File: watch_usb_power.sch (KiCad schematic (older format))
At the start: 31 parts, among them CON1 USB-MICRO-B, U4 74AHC1G14, U5 LTC4063, U6 FT230XQ, U7 TPS61093

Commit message: Added .gitignore, finished midmount layout
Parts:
- removed C28: 100nF, SMD_Packages:SMD-0603, symbol C
- removed C34: 1uF, SMD_Packages:SMD-0603, symbol C
- CON1: footprint Omat:USB_MICRO_AB_FEMALE -> Omat:USB_MICRO_B_FEMALE_MIDMOUNT
- F1: value PPTC -> MF-FSMF050X-2; footprint SMD_Packages:SMD-0805 -> SMD_Packages:SMD-0603
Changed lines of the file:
@@
 F 0 "CON1" H 1300 2300 50  0000 C CNN
 F 1 "USB-MICRO-B" H 1450 1600 50  0000 C CNN
-F 2 "Omat:USB_MICRO_AB_FEMALE" H 1600 1850 50  0001 C CNN
+F 2 "Omat:USB_MICRO_B_FEMALE_MIDMOUNT" H 1600 1850 50  0001 C CNN
 F 3 "" H 1600 1850 50  0000 C CNN
 	1    1600 1950
@@
 P 2650 1400
 F 0 "F1" H 2750 1450 40  0000 C CNN
-F 1 "PPTC" H 2550 1350 40  0000 C CNN
-F 2 "SMD_Packages:SMD-0805" H 2650 1400 60  0001 C CNN
+F 1 "MF-FSMF050X-2" H 2550 1350 40  0000 C CNN
+F 2 "SMD_Packages:SMD-0603" H 2650 1400 60  0001 C CNN
 F 3 "" H 2650 1400 60  0000 C CNN
 	1    2650 1400
@@
 Text Label 3500 2300 0    60   ~ 0
 VBUS
-$Comp
-L C C28
-U 1 1 5459F911
-P 4200 2650
-F 0 "C28" H 4200 2750 40  0000 L CNN
-F 1 "100nF" H 4206 2565 40  0000 L CNN
-F 2 "SMD_Packages:SMD-0603" H 4238 2500 30  0001 C CNN
-F 3 "" H 4200 2650 60  0000 C CNN
-	1    4200 2650
-	1    0    0    -1
-$EndComp
 $Comp
 L CP2 C27
@@
 	4800 2100 4500 2100
 Connection ~ 4500 2300
-Wire Wire Line
-	4200 2200 4800 2200
 Connection ~ 4500 2200
 Wire Wire Line
@@
 Connection ~ 4750 2550
 Wire Wire Line
-	4750 2950 4200 2950
-Wire Wire Line
 	4500 2850 4500 3050
 Connection ~ 4500 2950
@@
 	3500 2950 3500 3000
 Connection ~ 3500 2950
-Wire Wire Line
-	4200 2200 4200 2450
-Wire Wire Line
-	4200 2950 4200 2850
 Wire Wire Line
 	4500 2300 4800 2300
@@
 	7500 4950 7500 5200
 Wire Wire Line
-	7500 5200 10300 5200
-Wire Wire Line
 	7800 4900 7800 5200
 Connection ~ 7800 5200
@@
 Wire Wire Line
 	10200 3750 10200 3850
-Wire Wire Line
-	9350 3950 10450 3950
 Wire Wire Line
 	9350 4050 9650 4050
@@
 Connection ~ 9450 5200
 Connection ~ 9950 3950
-Connection ~ 9950 5200
 Wire Wire Line
 	8350 3900 8100 3900
@@
 	9350 4250 9450 4250
 Connection ~ 9450 4250
-Connection ~ 10300 3950
-Wire Wire Line
-	10300 3950 10300 4350
-Wire Wire Line
-	10300 5200 10300 4750
-$Comp
-L C C34
-U 1 1 545C5D16
-P 10300 4550
-F 0 "C34" H 10300 4650 40  0000 L CNN
-F 1 "1uF" H 10306 4465 40  0000 L CNN
-F 2 "SMD_Packages:SMD-0603" H 10338 4400 30  0001 C CNN
-F 3 "" H 10300 4550 60  0000 C CNN
-	1    10300 4550
-	1    0    0    -1
-$EndComp
+Wire Wire Line
+	4750 2950 4500 2950
+Wire Wire Line
+	4500 2200 4800 2200
+Wire Wire Line
+	9350 3950 10450 3950
+Wire Wire Line
+	7500 5200 9950 5200
 $EndSCHEMATC

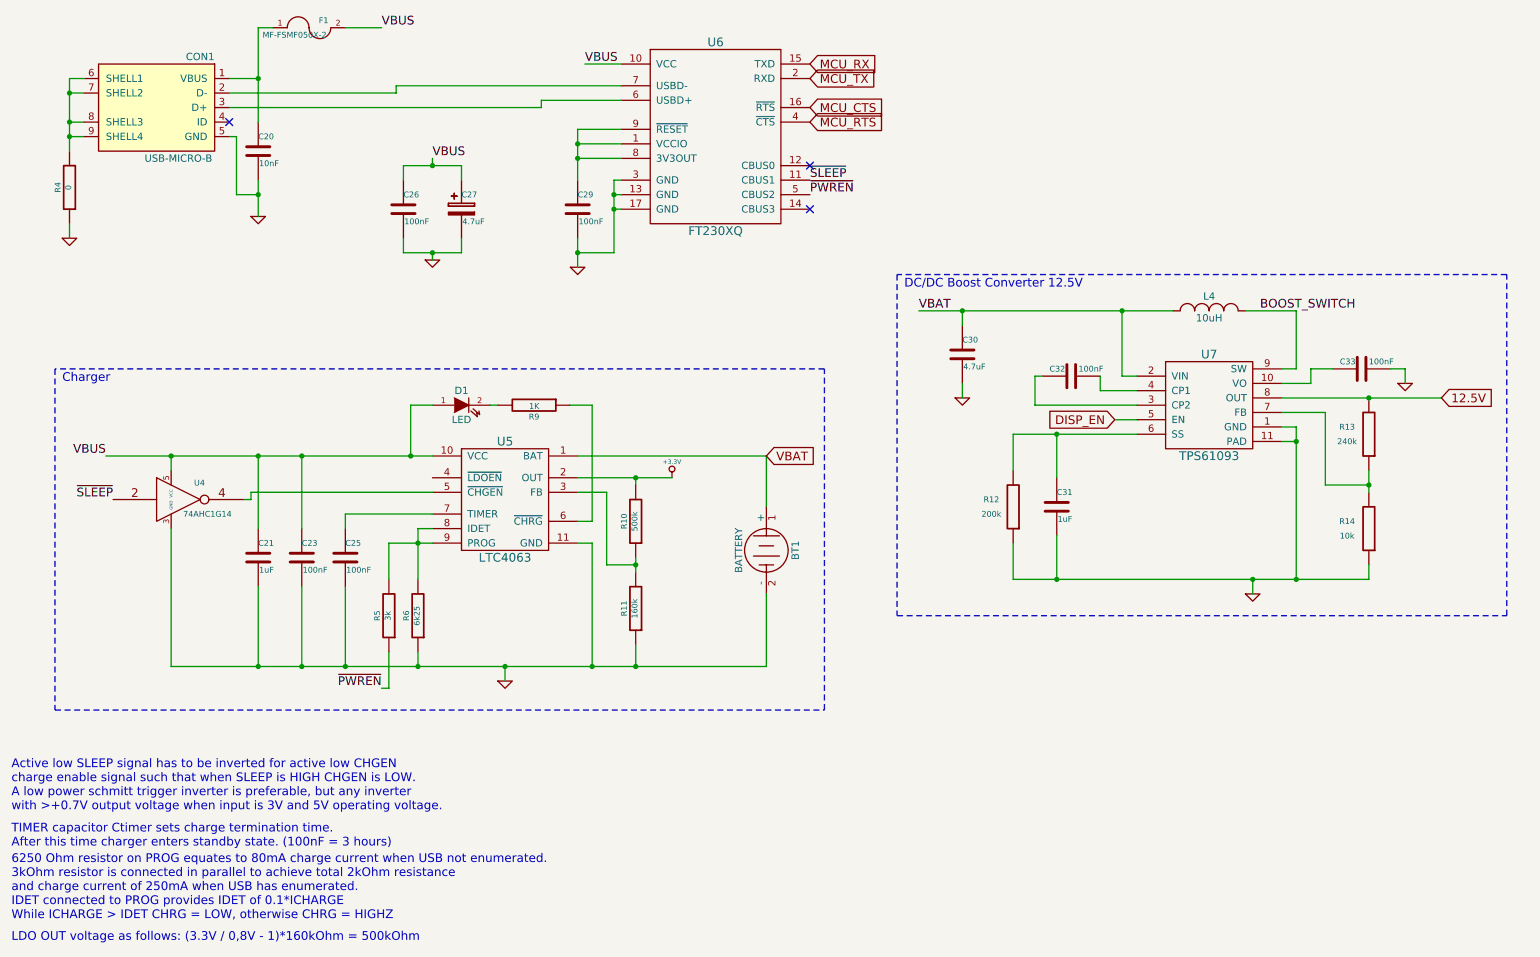
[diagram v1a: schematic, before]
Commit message: Added testpoints, adjusted silkscreen texts
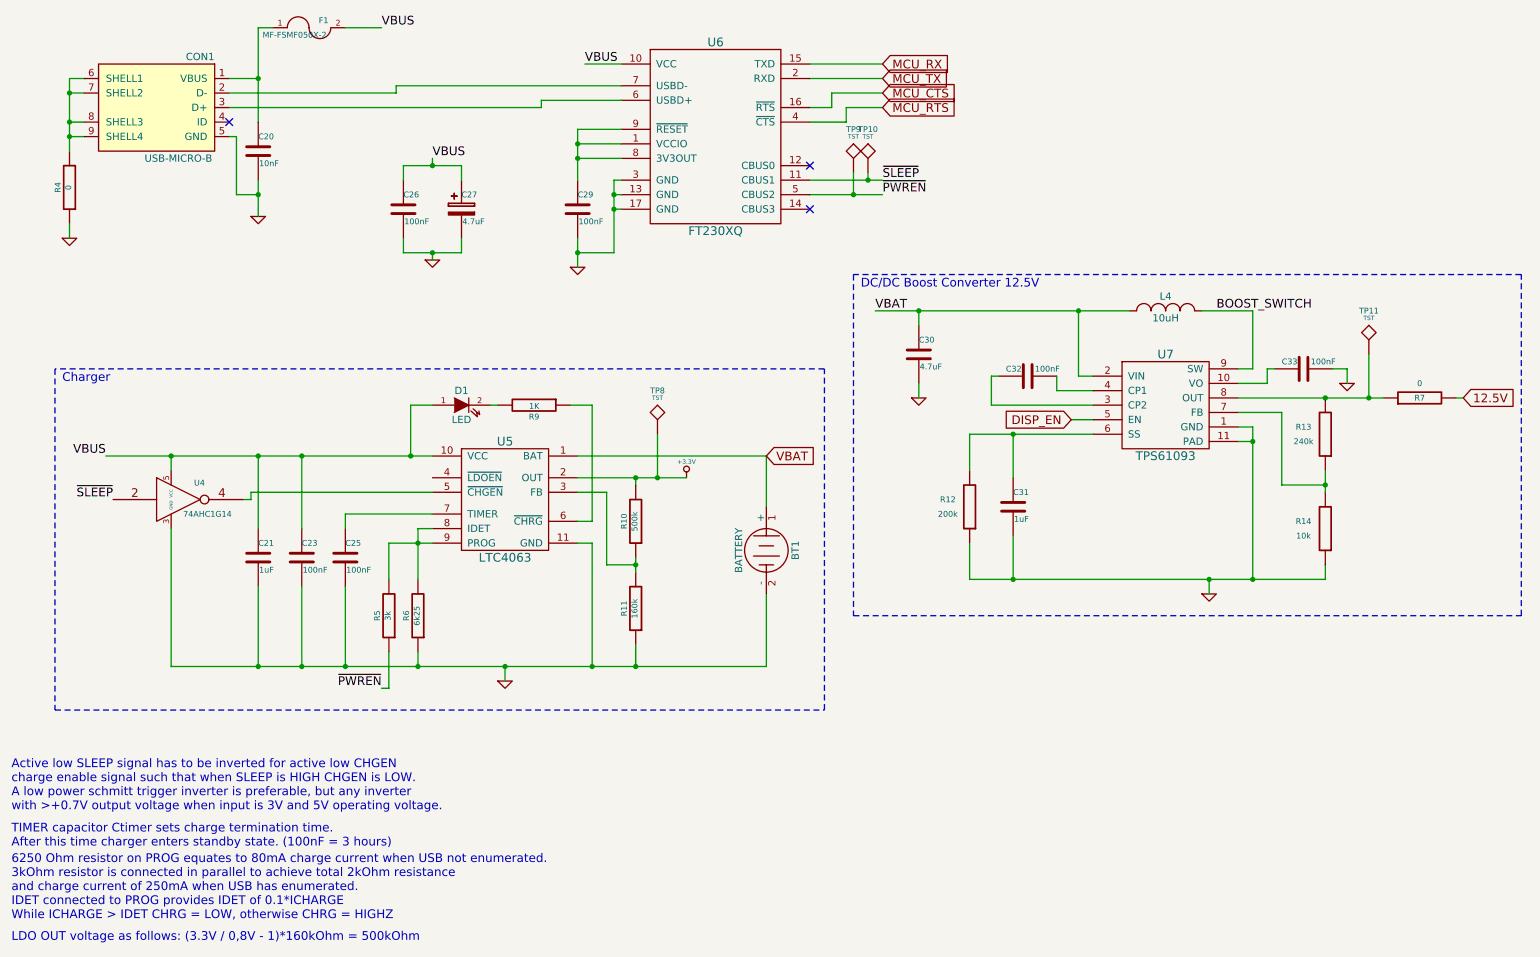
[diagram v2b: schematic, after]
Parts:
- added R7: 0, SMD_Packages:SMD-0603, symbol R
- added TP10, TP11, TP8, TP9: TST, Measurement_Points:Measurement_Point_Round-SMD-Pad_Small, symbol TST
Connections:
- net +3.3V: now also TP8.1
- net 12.5V: now also R7.2; no longer R13.2, U7.8 (OUT)
- net ~PWREN: now also TP9.1
- net ~SLEEP: now also TP10.1
- new net: R13.2, R7.1, TP11.1, U7.8 (OUT)
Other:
- moved on the sheet: C30, C31, C32, C33, L4, R12, R13, R14, U7

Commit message: Added missing 2.2uF cap to LTC4063 LDO output, normalized capacitor values to micro and pico, removed units from component values
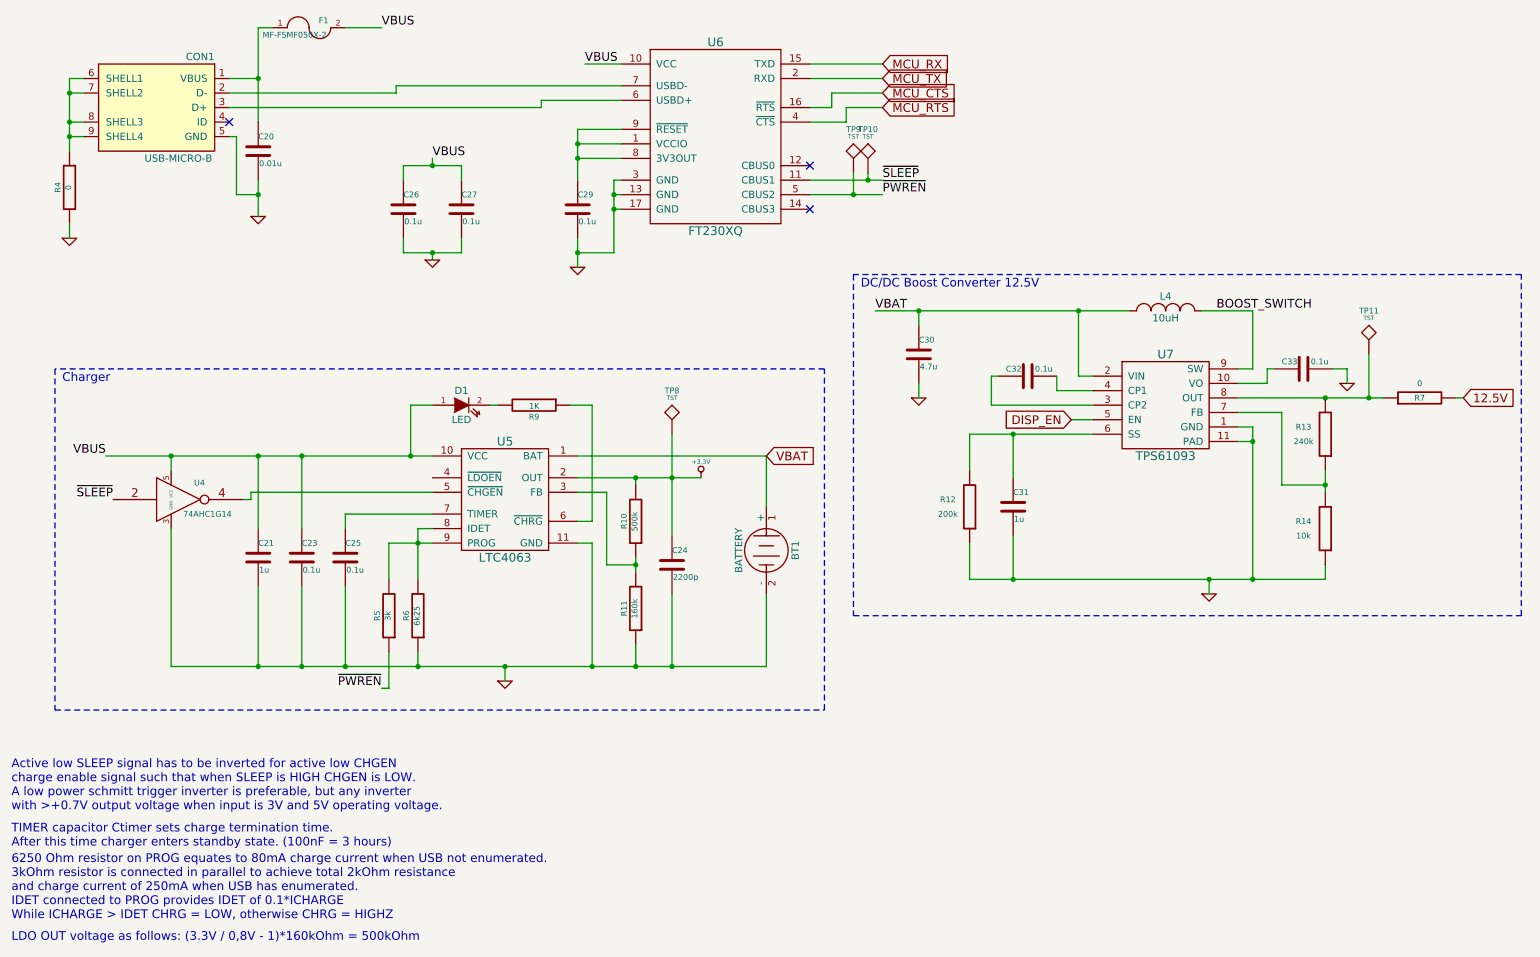
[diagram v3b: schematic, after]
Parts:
- removed C27: 4.7uF, SMD_Packages:SMD-0603, symbol CP2
- added C24: 2200p, SMD_Packages:SMD-0603, symbol C
- added C27: 0.1u, SMD_Packages:SMD-0603, symbol C
- C20: value 10nF -> 0.01u
- C21, C31: value 1uF -> 1u
- C23, C25, C26, C29, C32, C33: value 100nF -> 0.1u
- C30: value 4.7uF -> 4.7u
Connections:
- net +3.3V: now also C24.1
- net GND: now also C24.2, C27.2
- net VBUS: now also C27.1
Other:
- moved on the sheet: TP8
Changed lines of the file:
@@
 P 2300 2250
 F 0 "C20" H 2300 2350 40  0000 L CNN
-F 1 "10nF" H 2306 2165 40  0000 L CNN
+F 1 "0.01u" H 2306 2165 40  0000 L CNN
 F 2 "SMD_Packages:SMD-0603" H 2338 2100 30  0001 C CNN
 F 3 "" H 2300 2250 60  0000 C CNN
@@
 P 4500 2650
 F 0 "C29" H 4500 2750 40  0000 L CNN
-F 1 "100nF" H 4506 2565 40  0000 L CNN
+F 1 "0.1u" H 4506 2565 40  0000 L CNN
 F 2 "SMD_Packages:SMD-0603" H 4538 2500 30  0001 C CNN
 F 3 "" H 4500 2650 60  0000 C CNN
@@
 P 3300 2650
 F 0 "C26" H 3300 2750 40  0000 L CNN
-F 1 "100nF" H 3306 2565 40  0000 L CNN
+F 1 "0.1u" H 3306 2565 40  0000 L CNN
 F 2 "SMD_Packages:SMD-0603" H 3338 2500 30  0001 C CNN
 F 3 "" H 3300 2650 60  0000 C CNN
@@
 VBUS
 $Comp
-L CP2 C27
-U 1 1 5459FD49
-P 3700 2650
-F 0 "C27" H 3700 2750 40  0000 L CNN
-F 1 "4.7uF" H 3706 2565 40  0000 L CNN
-F 2 "SMD_Packages:SMD-0603" H 3738 2500 30  0001 C CNN
-F 3 "" H 3700 2650 60  0000 C CNN
-	1    3700 2650
-	1    0    0    -1
-$EndComp
-$Comp
 L C C23
 U 1 1 545A029E
 P 2600 5050
 F 0 "C23" H 2600 5150 40  0000 L CNN
-F 1 "100nF" H 2606 4965 40  0000 L CNN
+F 1 "0.1u" H 2606 4965 40  0000 L CNN
 F 2 "SMD_Packages:SMD-0603" H 2638 4900 30  0001 C CNN
 F 3 "" H 2600 5050 60  0000 C CNN
@@
 P 2900 5050
 F 0 "C25" H 2900 5150 40  0000 L CNN
-F 1 "100nF" H 2906 4965 40  0000 L CNN
+F 1 "0.1u" H 2906 4965 40  0000 L CNN
 F 2 "SMD_Packages:SMD-0603" H 2938 4900 30  0001 C CNN
 F 3 "" H 2900 5050 60  0000 C CNN
@@
 P 2300 5050
 F 0 "C21" H 2300 5150 40  0000 L CNN
-F 1 "1uF" H 2306 4965 40  0000 L CNN
+F 1 "1u" H 2306 4965 40  0000 L CNN
 F 2 "SMD_Packages:SMD-0603" H 2338 4900 30  0001 C CNN
 F 3 "" H 2300 5050 60  0000 C CNN
@@
 P 6850 3650
 F 0 "C30" H 6850 3750 40  0000 L CNN
-F 1 "4.7uF" H 6856 3565 40  0000 L CNN
+F 1 "4.7u" H 6856 3565 40  0000 L CNN
 F 2 "SMD_Packages:SMD-0603" H 6888 3500 30  0001 C CNN
 F 3 "" H 6850 3650 60  0000 C CNN
@@
 P 7600 3800
 F 0 "C32" V 7550 3650 40  0000 L CNN
-F 1 "100nF" V 7550 3850 40  0000 L CNN
+F 1 "0.1u" V 7550 3850 40  0000 L CNN
 F 2 "SMD_Packages:SMD-0603" H 7638 3650 30  0001 C CNN
 F 3 "" H 7600 3800 60  0000 C CNN
@@
 P 7500 4700
 F 0 "C31" H 7500 4800 40  0000 L CNN
-F 1 "1uF" H 7506 4615 40  0000 L CNN
+F 1 "1u" H 7506 4615 40  0000 L CNN
 F 2 "SMD_Packages:SMD-0603" H 7538 4550 30  0001 C CNN
 F 3 "" H 7500 4700 60  0000 C CNN
@@
 P 9500 3750
 F 0 "C33" V 9450 3600 40  0000 L CNN
-F 1 "100nF" V 9450 3800 40  0000 L CNN
+F 1 "0.1u" V 9450 3800 40  0000 L CNN
 F 2 "SMD_Packages:SMD-0603" H 9538 3600 30  0001 C CNN
 F 3 "" H 9500 3750 60  0000 C CNN
@@
 L +3.3V #PWR024
 U 1 1 546AD98B
-P 5250 4500
-F 0 "#PWR024" H 5250 4460 30  0001 C CNN
-F 1 "+3.3V" H 5250 4610 30  0000 C CNN
-F 2 "" H 5250 4500 60  0000 C CNN
-F 3 "" H 5250 4500 60  0000 C CNN
-	1    5250 4500
+P 5350 4500
+F 0 "#PWR024" H 5350 4460 30  0001 C CNN
+F 1 "+3.3V" H 5350 4610 30  0000 C CNN
+F 2 "" H 5350 4500 60  0000 C CNN
+F 3 "" H 5350 4500 60  0000 C CNN
+	1    5350 4500
 	1    0    0    -1
 $EndComp
@@
 	4900 4500 4900 4550
 Wire Wire Line
-	4500 4500 5250 4500
+	4500 4500 5350 4500
 Wire Wire Line
 	4500 4600 4700 4600
@@
 L TST TP8
 U 1 1 54824541
-P 5050 4200
-F 0 "TP8" H 5050 4500 40  0000 C CNN
-F 1 "TST" H 5050 4450 30  0000 C CNN
-F 2 "Measurement_Points:Measurement_Point_Round-SMD-Pad_Small" H 5050 4200 60  0001 C CNN
-F 3 "" H 5050 4200 60  0000 C CNN
-	1    5050 4200
-	1    0    0    -1
-$EndComp
-Wire Wire Line
-	5050 4200 5050 4500
-Connection ~ 5050 4500
+P 5150 4200
+F 0 "TP8" H 5150 4500 40  0000 C CNN
+F 1 "TST" H 5150 4450 30  0000 C CNN
+F 2 "Measurement_Points:Measurement_Point_Round-SMD-Pad_Small" H 5150 4200 60  0001 C CNN
+F 3 "" H 5150 4200 60  0000 C CNN
+	1    5150 4200
+	1    0    0    -1
+$EndComp
+Wire Wire Line
+	5150 4200 5150 4900
+Connection ~ 5150 4500
 $Comp
 L TST TP11
@@
 	0    -1   -1   0
 $EndComp
+$Comp
+L C C24
+U 1 1 54839CDB
+P 5150 5100
+F 0 "C24" H 5150 5200 40  0000 L CNN
+F 1 "2200p" H 5156 5015 40  0000 L CNN
+F 2 "SMD_Packages:SMD-0603" H 5188 4950 30  0001 C CNN
+F 3 "" H 5150 5100 60  0000 C CNN
+	1    5150 5100
+	1    0    0    -1
+$EndComp
+Wire Wire Line
+	5150 5300 5150 5800
+Connection ~ 5150 5800
+$Comp
+L C C27
+U 1 1 5483AE74
+P 3700 2650
+F 0 "C27" H 3700 2750 40  0000 L CNN
+F 1 "0.1u" H 3706 2565 40  0000 L CNN
+F 2 "SMD_Packages:SMD-0603" H 3738 2500 30  0001 C CNN
+F 3 "" H 3700 2650 60  0000 C CNN
+	1    3700 2650
+	1    0    0    -1
+$EndComp
 $EndSCHEMATC

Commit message: Fixed footprints for MCU and USB-UART, added testpoints
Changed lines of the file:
@@
 EESchema Schematic File Version 2
+LIBS:watch-rescue
 LIBS:power
 LIBS:device
@@
 $EndComp
 $Comp
-L GND #PWR016
+L GND-RESCUE-watch #PWR016
 U 1 1 5459B57E
 P 2300 2700
+AR Path="/5459B57E" Ref="#PWR016"  Part="1"
+AR Path="/5459B076/5459B57E" Ref="#PWR016"  Part="1"
 F 0 "#PWR016" H 2300 2700 30  0001 C CNN
 F 1 "GND" H 2300 2630 30  0001 C CNN
@@
 $EndComp
 $Comp
-L GND #PWR017
+L GND-RESCUE-watch #PWR017
 U 1 1 5459E8BE
 P 4500 3050
+AR Path="/5459E8BE" Ref="#PWR017"  Part="1"
+AR Path="/5459B076/5459E8BE" Ref="#PWR017"  Part="1"
 F 0 "#PWR017" H 4500 3050 30  0001 C CNN
 F 1 "GND" H 4500 2980 30  0001 C CNN
@@
 $EndComp
 $Comp
-L GND #PWR018
+L GND-RESCUE-watch #PWR018
 U 1 1 5459F2E2
 P 3500 3000
+AR Path="/5459F2E2" Ref="#PWR018"  Part="1"
+AR Path="/5459B076/5459F2E2" Ref="#PWR018"  Part="1"
 F 0 "#PWR018" H 3500 3000 30  0001 C CNN
 F 1 "GND" H 3500 2930 30  0001 C CNN
@@
 $EndComp
 $Comp
-L GND #PWR019
+L GND-RESCUE-watch #PWR019
 U 1 1 545A06F4
 P 1000 2850
+AR Path="/545A06F4" Ref="#PWR019"  Part="1"
+AR Path="/5459B076/545A06F4" Ref="#PWR019"  Part="1"
 F 0 "#PWR019" H 1000 2850 30  0001 C CNN
 F 1 "GND" H 1000 2780 30  0001 C CNN
@@
 $EndComp
 $Comp
-L GND #PWR020
+L GND-RESCUE-watch #PWR020
 U 1 1 545A3138
 P 4000 5900
+AR Path="/545A3138" Ref="#PWR020"  Part="1"
+AR Path="/5459B076/545A3138" Ref="#PWR020"  Part="1"
 F 0 "#PWR020" H 4000 5900 30  0001 C CNN
 F 1 "GND" H 4000 5830 30  0001 C CNN
@@
 $EndComp
 $Comp
-L GND #PWR021
+L GND-RESCUE-watch #PWR021
 U 1 1 545C29FC
 P 6850 3950
+AR Path="/545C29FC" Ref="#PWR021"  Part="1"
+AR Path="/5459B076/545C29FC" Ref="#PWR021"  Part="1"
 F 0 "#PWR021" H 6850 3950 30  0001 C CNN
 F 1 "GND" H 6850 3880 30  0001 C CNN
@@
 $EndComp
 $Comp
-L GND #PWR022
+L GND-RESCUE-watch #PWR022
 U 1 1 545C4334
 P 8850 5300
+AR Path="/545C4334" Ref="#PWR022"  Part="1"
+AR Path="/5459B076/545C4334" Ref="#PWR022"  Part="1"
 F 0 "#PWR022" H 8850 5300 30  0001 C CNN
 F 1 "GND" H 8850 5230 30  0001 C CNN
@@
 $EndComp
 $Comp
-L GND #PWR023
+L GND-RESCUE-watch #PWR023
 U 1 1 545C508F
 P 9800 3850
+AR Path="/545C508F" Ref="#PWR023"  Part="1"
+AR Path="/5459B076/545C508F" Ref="#PWR023"  Part="1"
 F 0 "#PWR023" H 9800 3850 30  0001 C CNN
 F 1 "GND" H 9800 3780 30  0001 C CNN
@@
 	9050 4150 9150 4150
 Wire Wire Line
-	9150 5200 9150 4150
+	9150 4150 9150 5200
 Connection ~ 8850 5200
 Wire Wire Line
